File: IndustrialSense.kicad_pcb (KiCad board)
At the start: 4 copper layers, 46.9 x 90 mm, 111 parts, among them CN2 B4B-ZR (LF)(SN), CN3 ZH1.5-6P-LT, CN4 B4B-ZR (LF)(SN), J5 Conn_01x10_Socket, J6 Conn_01x10_Socket, Q1 SISA14DN-T1-GE3, Q13 MMBT3904, Q15 LMBT3904DW1T1G, Q2 SISA14DN-T1-GE3, Q3 SISA14DN-T1-GE3, Q4 SISA14DN-T1-GE3, Q5 CEM4435A, Q6 CH221K, SW2 SKRKAEE020, SW3 SKRKAEE020, U1 ESP32-S3-WROOM-1U-N16, U10 LM74700QDBVRQ1, U11 CN3795, U12 XFL4020-222MEC_C122469, U13 B6B-ZR (LF)(SN), U14 CH334F, U15 TPS3831G33DQNR, U17 THVD1406DR, U2 B6B-ZR (LF)(SN), U3 CH343P, U4 MAX17049G+T10, U5 LM74700QDBVRQ1, U6 LM74700QDBVRQ1, U7 TPS62132RGTT, U8 LM74700QDBVRQ1, U9 XC6209F332MR-G, X1 X322512MSB4SI

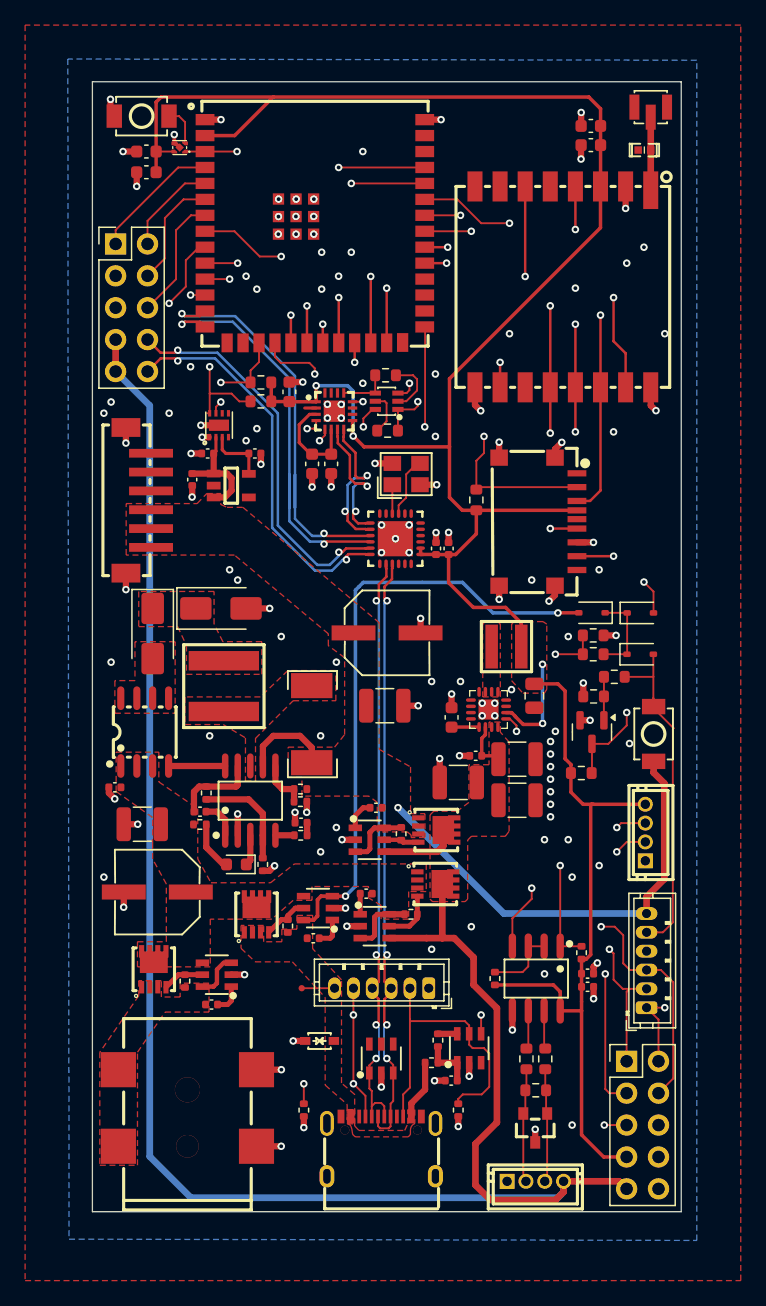
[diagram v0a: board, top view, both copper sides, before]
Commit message: [Schematic/PCB][Added] Testpoints test 2
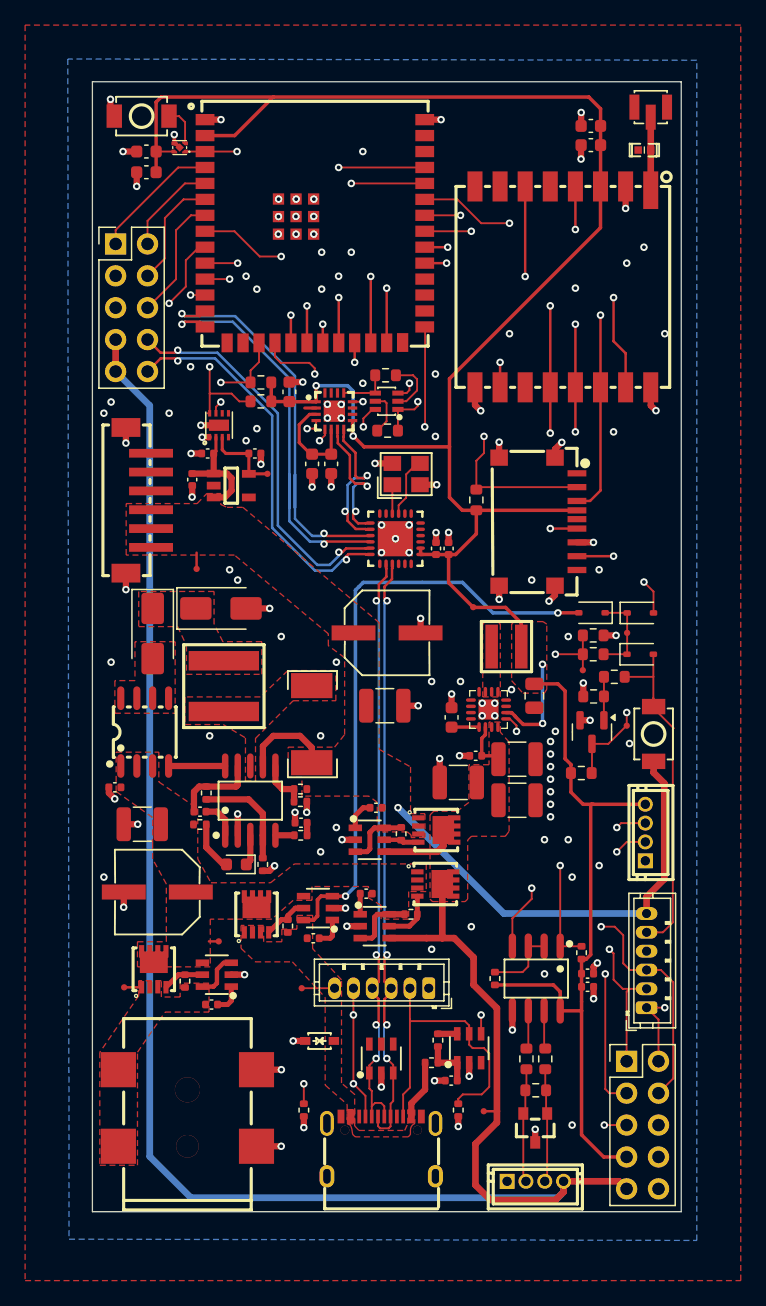
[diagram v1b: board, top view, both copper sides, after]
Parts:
- added TP10: TestPoint, tests:tp05, F.Cu at (163.6, 94.1)
- added TP2: TestPoint, tests:tp05, F.Cu at (138.4, 78.4)
- added TP3: TestPoint, tests:tp05, F.Cu at (132.8, 86.0)
- added TP4: TestPoint, tests:tp05, F.Cu at (154.8, 89.0)
- added TP5: TestPoint, tests:tp05, F.Cu at (127.0, 119.3)
- added TP6: TestPoint, tests:tp05, F.Cu at (134.6, 115.7)
- added TP7: TestPoint, tests:tp05, F.Cu at (141.2, 119.4)
- added TP8: TestPoint, tests:tp05, F.Cu at (167.1, 98.5)
- added TP9: TestPoint, tests:tp05, F.Cu at (167.1, 91.1)
- moved TP1 17.5 mm to (155.7, 129.2)
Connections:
- net Net-(D6-K) renamed /Project Architecture/Power Management/PWR_SEL
- net Net-(U7-EN) renamed /Project Architecture/Power Management/PWR_EN
- TP1 pad 1: VBUS -> V_MAIN
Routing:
- net 3V3_FG: track 4.87 -> 6.35 mm
- net VSUN: track 3.82 -> 5.22 mm
- net V_BAT: track 58.4 -> 59.7 mm
- net /Project Architecture/Power Management/PWR_EN: track 14.4 -> 15.7 mm
- net V_MAIN: track 156.8 -> 157.8 mm
- net V_CHRG: track 12.9 -> 13.7 mm
